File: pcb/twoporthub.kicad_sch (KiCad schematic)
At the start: 0 parts

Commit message: Imported a lot of models, and wrote up schematic for two upstream nodes and a switch
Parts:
- added J1, J2, J3: USB_C_16P, symbol KiCad-User:USB_C_Receptacle_USB2.0_16P
- added J4: USB_C_Receptacle_USB2.0_16P, symbol KiCad-User:USB_C_Receptacle_USB2.0_16P
- added J6: USB_A, symbol Connector:USB_A
- added R1, R2: 5.1kΩ, symbol Device:R
- added R3, R4: 56kΩ, symbol Device:R
- added U1: SL2.1A, Package_SO:SOIC-16_4.55x10.3mm_P1.27mm, symbol sl2.1a:SL2.1A
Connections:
- new net: J2.A5 (CC1), R3.2
- new net: J1.A5 (CC1), R1.2
- new net: J1.B5 (CC2), R2.2
- new net +5V: J1.A4 (VBUS), J1.A9 (VBUS), J1.B4 (VBUS), J1.B9 (VBUS), J2.A4 (VBUS), J2.A9 (VBUS), J2.B4 (VBUS), J2.B9 (VBUS), J3.A4 (VBUS), J3.A9 (VBUS), J3.B4 (VBUS), J3.B9 (VBUS), J4.A4 (VBUS), J4.A9 (VBUS), J4.B4 (VBUS), J4.B9 (VBUS), J6.1 (VBUS), R3.1, U1.11 (VCC5V)
- new net D+: J1.A6 (D+), J1.B6 (D+), U1.10 (UDP)
- new net D-: J1.A7 (D-), J1.B7 (D-), U1.9 (UDM)
- new net D1+: J2.A6 (D+), J2.B6 (D+), U1.8 (DP1)
- new net D1-: J2.A7 (D-), J2.B7 (D-), U1.7 (DM1)
- new net D2+: J3.A6 (D+), J3.B6 (D+), U1.6 (DP2)
- new net D2-: J3.A7 (D-), J3.B7 (D-), U1.5 (DM2)
- new net D3+: J4.A6 (D+), J4.B6 (D+), U1.4 (DP3)
- new net D3-: J4.A7 (D-), J4.B7 (D-), U1.3 (DM3)
- new net D4+: J6.3 (D+), U1.2 (DP4)
- new net D4-: J6.2 (D-), U1.1 (DM4)
- new net GND: J1.A1 (GND), J1.A12 (GND), J1.B1 (GND), J1.B12 (GND), J1.SH (SHIELD), J2.A1 (GND), J2.A12 (GND), J2.B1 (GND), J2.B12 (GND), J2.SH (SHIELD), J3.A1 (GND), J3.A12 (GND), J3.B1 (GND), J3.B12 (GND), J3.SH (SHIELD), J4.A1 (GND), J4.A12 (GND), J4.B1 (GND), J4.B12 (GND), J4.SH (SHIELD), J6.4 (GND), J6.SH (Shield), R1.1, R2.1, U1.12 (GND), U1.16 (XIN)
- no-connect marks 0 -> 9
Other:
- note added: "Chip Pinout"
- note added: "USBA Out 4"
- note added: "USBC In"
- note added: "USBC Out 1"
- note added: "USBC Out 2"
- note added: "USBC Out 3"

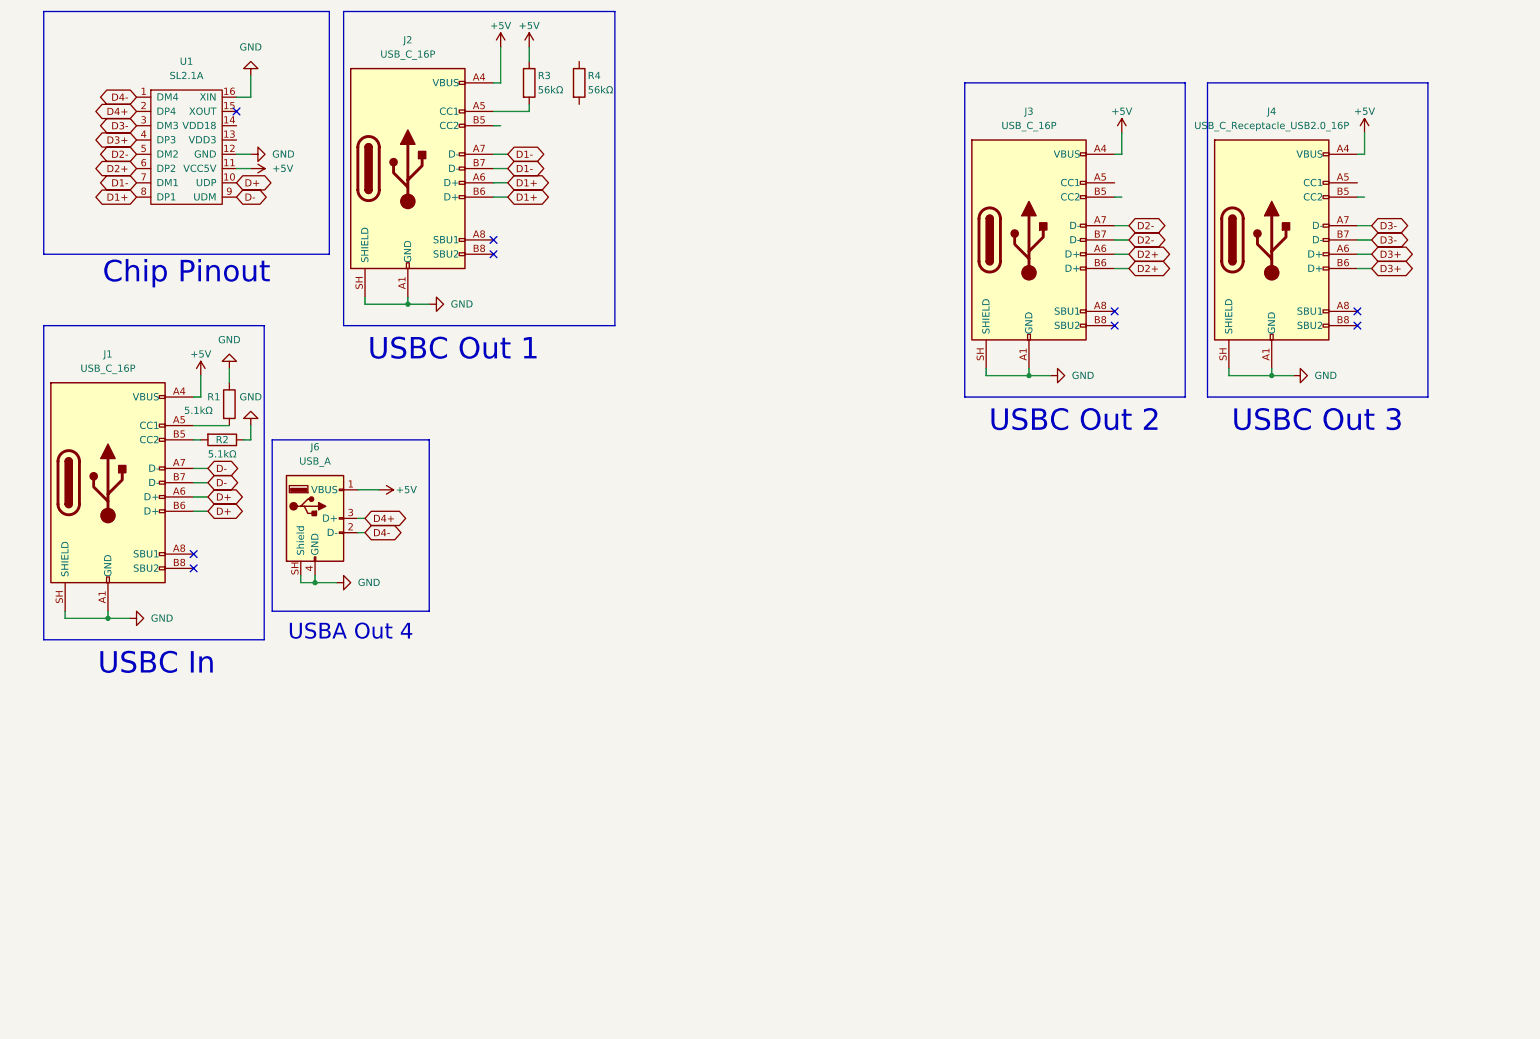
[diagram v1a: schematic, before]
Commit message: Added esd protection to one poirt so far
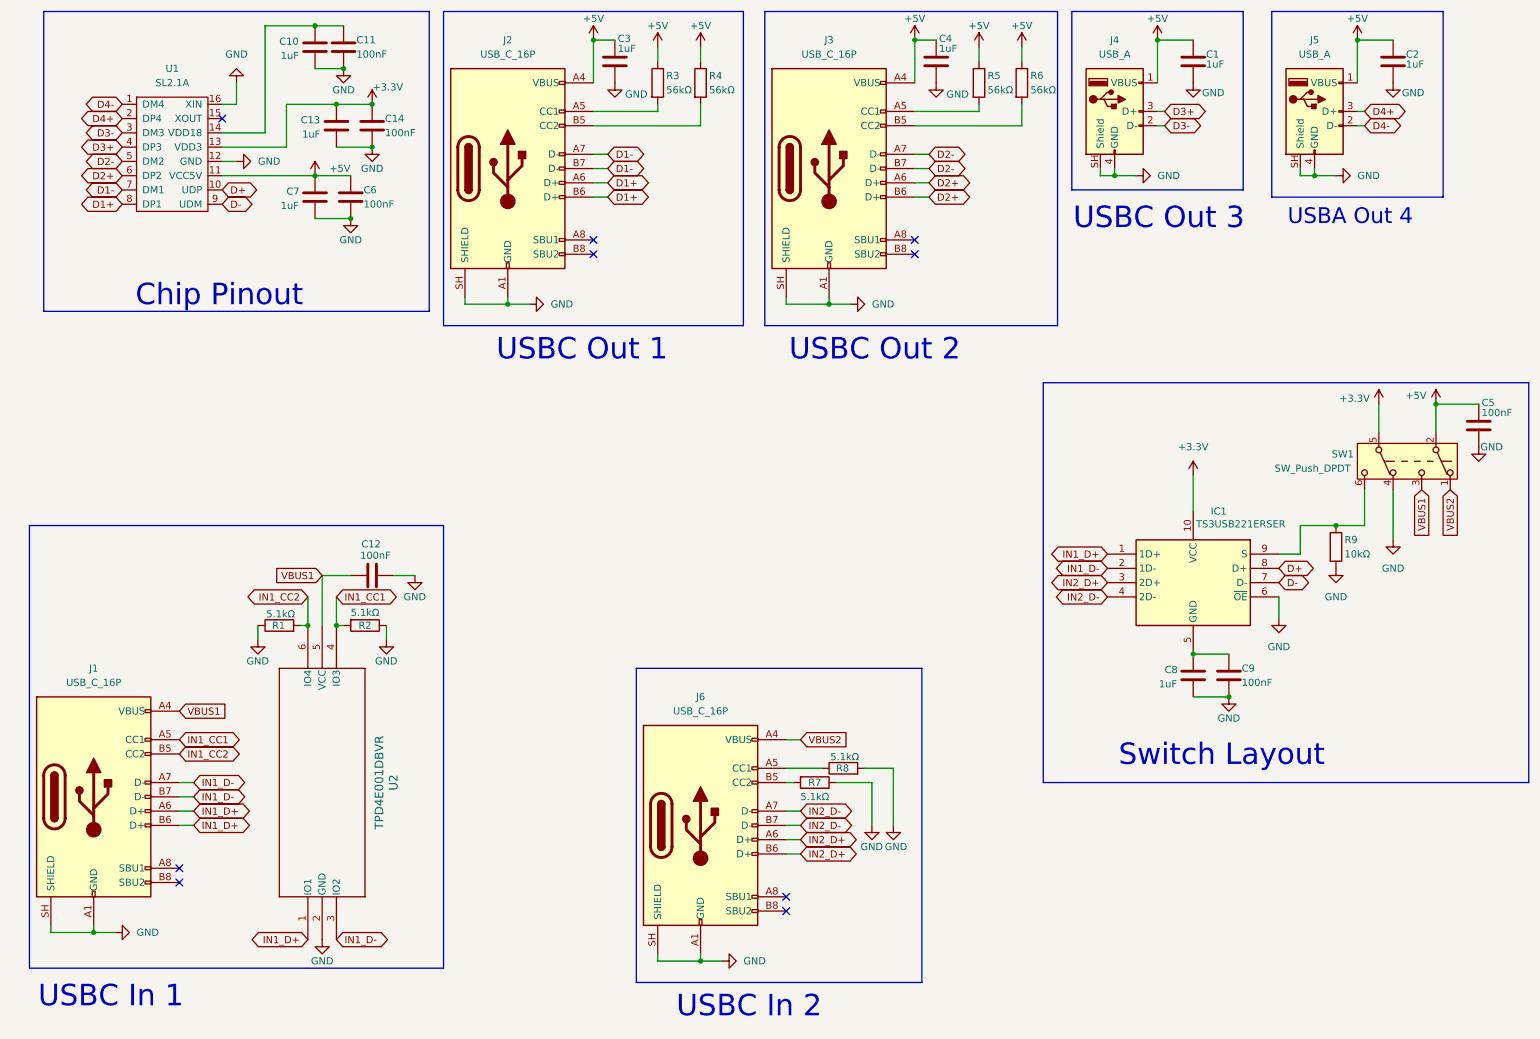
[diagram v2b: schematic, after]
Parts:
- removed J4: USB_C_Receptacle_USB2.0_16P, symbol KiCad-User:USB_C_Receptacle_USB2.0_16P
- added C1, C10, C13, C2, C3, C4, C7, C8: 1uF, symbol Device:C
- added C11, C12, C14, C5, C6, C9: 100nF, symbol Device:C
- added IC1: TS3USB221ERSER, TS3USB221ERSER, symbol Project:TS3USB221ERSER
- added J4: USB_A, symbol Connector:USB_A
- added J6: USB_C_16P, symbol KiCad-User:USB_C_Receptacle_USB2.0_16P
- added R5, R6: 56kΩ, symbol Device:R
- added R7, R8: 5.1kΩ, symbol Device:R
- added R9: 10kΩ, symbol Device:R
- added SW1: SW_Push_DPDT, symbol Switch:SW_Push_DPDT
- added U2: TPD4E001DBVR, DBV6, symbol Project:TPD4E001DBVR
- renumbered J6 to J5
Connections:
- net +5V: now also R4.1, C1.1, C2.1, C3.1, C4.1, C5.1, C6.1, C7.1, J4.1 (VBUS), R5.1, R6.1, SW1.2 (B); no longer J1.A4 (VBUS), J1.A9 (VBUS), J1.B4 (VBUS), J1.B9 (VBUS)
- net D+: now also IC1.8 (D+); no longer J1.A6 (D+), J1.B6 (D+)
- net D-: now also IC1.7 (D-); no longer J1.A7 (D-), J1.B7 (D-)
- net D3+: now also J4.3 (D+)
- net D3-: now also J4.2 (D-)
- net GND: now also C1.2, C10.2, C11.2, C12.2, C13.2, C14.2, C2.2, C3.2, C4.2, C5.2, C6.2, C7.2, C8.2, C9.2, IC1.6 (~{OE}), J4.4 (GND), J4.SH (Shield), J6.A1 (GND), J6.A12 (GND), J6.B1 (GND), J6.B12 (GND), J6.SH (SHIELD), R7.1, R8.2, R9.2, SW1.4 (A), U2.2 (GND)
- net +3.3V: now reaches U1.13 (VDD3)
- net +3.3V: now also C13.1, C14.1, IC1.10 (VCC), SW1.5 (B)
- net at U1.14 (VDD18): now also C10.1, C11.1
- net at R4.2: now also J2.B5 (CC2)
- net IN1_CC1: now reaches J1.A5 (CC1)
- net IN1_CC1: now also R2.2, U2.4 (IO3); no longer R1.2
- net at J3.A5 (CC1): now also R5.2
- net at J3.B5 (CC2): now also R6.2
- net IN1_CC2: now reaches J1.B5 (CC2)
- net IN1_CC2: now also R1.2, U2.6 (IO4); no longer R2.2
- new net: C8.1, C9.1, IC1.5 (GND)
- new net: IC1.9 (S), R9.1, SW1.6 (C)
- new net: J6.B5 (CC2), R7.2
- new net: J6.A5 (CC1), R8.1
- new net IN1_D+: IC1.1 (1D+), J1.A6 (D+), J1.B6 (D+), U2.1 (IO1)
- new net IN1_D-: IC1.2 (1D-), J1.A7 (D-), J1.B7 (D-), U2.3 (IO2)
- new net IN2_D+: IC1.3 (2D+), J6.A6 (D+), J6.B6 (D+)
- new net IN2_D-: IC1.4 (2D-), J6.A7 (D-), J6.B7 (D-)
- new net VBUS1: C12.1, J1.A4 (VBUS), J1.A9 (VBUS), J1.B4 (VBUS), J1.B9 (VBUS), SW1.3 (C), U2.5 (VCC)
- new net VBUS2: J6.A4 (VBUS), J6.A9 (VBUS), J6.B4 (VBUS), J6.B9 (VBUS), SW1.1 (A)
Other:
- note added: "Switch Layout"
- note added: "USBC In 1"
- note added: "USBC In 2"
- note removed: "USBC In"
- moved on the sheet: J2, J3, J5, R3, R4, U1
